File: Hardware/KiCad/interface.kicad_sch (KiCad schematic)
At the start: 34 parts, among them J1 USB_C, J2 STLink, J6 UART, J7 OLED, SW10 SW_Push_45deg, SW11 SW_Push_45deg, SW12 SW_Push_45deg, SW13 SW_Push_45deg, SW14 SW_Push_45deg, SW15 SW_Push_45deg, SW16 SW_Push_45deg, SW17 SW_Push_45deg, SW2 SW_Push_45deg, SW3 SW_Push_45deg, SW4 SW_Push_45deg, SW5 SW_Push_45deg, SW6 SW_Push_45deg, SW7 SW_Push_45deg, SW8 SW_Push_45deg, SW9 SW_Push_45deg, U1 USBLC6-2

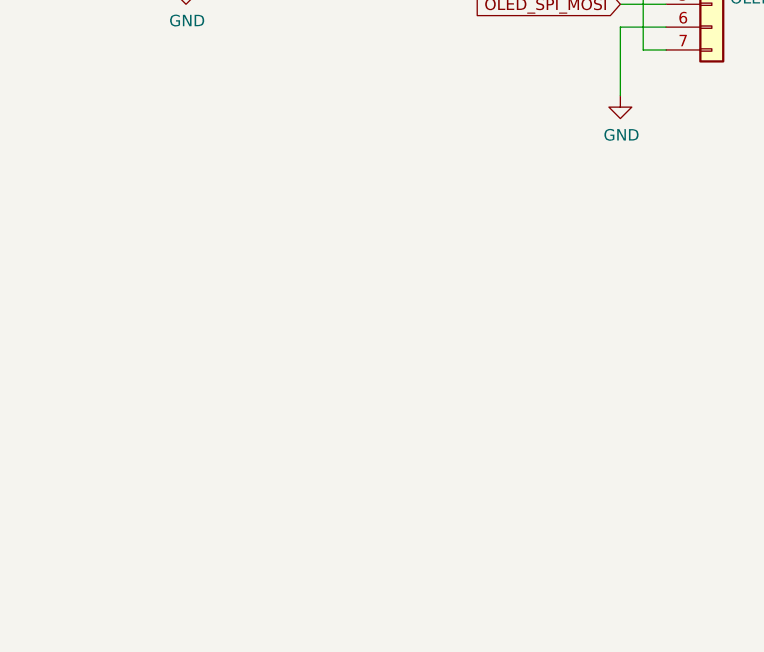
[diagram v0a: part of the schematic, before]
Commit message: add encoder & volume control, move SD_DET to accommodate encoder
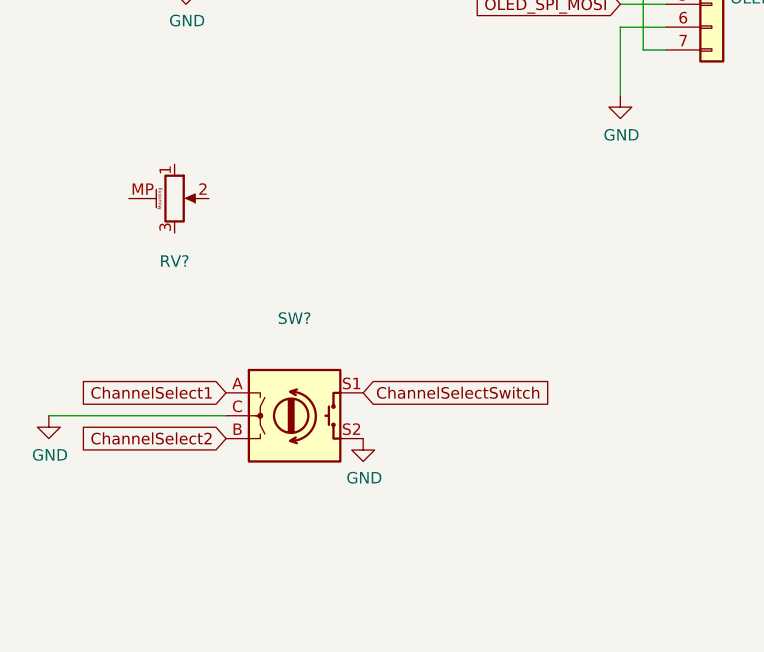
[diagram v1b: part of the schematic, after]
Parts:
- added RV?: (no value), symbol Device:R_Potentiometer_MountingPin
- added SW?: (no value), symbol Device:RotaryEncoder_Switch
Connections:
- net GND: now also SW?.C, SW?.S2
- new net ChannelSelect1: SW?.A
- new net ChannelSelect2: SW?.B
- new net ChannelSelectSwitch: SW?.S1
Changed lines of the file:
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@@
     (stroke (width 0) (type solid) (color 0 0 0 0))
+  )
+  (wire (pts (xy 25.4 91.44) (xy 45.085 91.44))
+    (stroke (width 0) (type default) (color 0 0 0 0))
   )
   (wire (pts (xy 58.42 143.51) (xy 58.42 156.21))
@@
     )
   )
+  (global_label "ChannelSelect2" (shape input) (at 45.085 93.98 180) (fields_autoplaced)
+    (effects (font (size 1.27 1.27)) (justify right))
+    (property "Intersheet References" "${INTERSHEET_REFS}" (id 0) (at 27.9762 93.9006 0)
+      (effects (font (size 1.27 1.27)) (justify right) hide)
+    )
+  )
   (global_label "C2" (shape output) (at 43.18 135.89 90) (fields_autoplaced)
     (effects (font (size 1.27 1.27)) (justify left))
@@
     )
   )
+  (global_label "ChannelSelectSwitch" (shape input) (at 60.325 88.9 0) (fields_autoplaced)
+    (effects (font (size 1.27 1.27)) (justify left))
+    (property "Intersheet References" "${INTERSHEET_REFS}" (id 0) (at 82.3324 88.8206 0)
+      (effects (font (size 1.27 1.27)) (justify left) hide)
+    )
+  )
   (global_label "OLED_SPI_MOSI" (shape input) (at 88.9 45.72 180) (fields_autoplaced)
     (effects (font (size 1.27 1.27)) (justify right))
@@
     )
   )
+  (global_label "ChannelSelect1" (shape input) (at 45.085 88.9 180) (fields_autoplaced)
+    (effects (font (size 1.27 1.27)) (justify right))
+    (property "Intersheet References" "${INTERSHEET_REFS}" (id 0) (at 27.9762 88.8206 0)
+      (effects (font (size 1.27 1.27)) (justify right) hide)
+    )
+  )
   (global_label "C1" (shape output) (at 27.94 135.89 90) (fields_autoplaced)
     (effects (font (size 1.27 1.27)) (justify left))
@@
     (pin "1")
     (pin "2")
+  )
+  (symbol (lib_id "Device:RotaryEncoder_Switch") (at 52.705 91.44 0) (unit 1)
+    (in_bom yes) (on_board yes) (fields_autoplaced)
+    (property "Reference" "SW?" (id 0) (at 52.705 80.645 0))
+    (property "Value" "" (id 1) (at 52.705 83.185 0))
+    (property "Footprint" "" (id 2) (at 48.895 87.376 0)
+      (effects (font (size 1.27 1.27)) hide)
+    )
+    (property "Datasheet" "https://www.cuidevices.com/product/resource/acz11.pdf" (id 3) (at 52.705 84.836 0)
+      (effects (font (size 1.27 1.27)) hide)
+    )
+    (pin "A")
+    (pin "B")
+    (pin "C")
+    (pin "S1")
+    (pin "S2")
   )
   (symbol (lib_id "power:VDD") (at 146.05 20.32 0) (unit 1)
@@
     (pin "2")
   )
+  (symbol (lib_id "Device:R_Potentiometer_MountingPin") (at 39.37 67.31 0) (unit 1)
+    (in_bom yes) (on_board yes)
+    (property "Reference" "RV?" (id 0) (at 39.37 74.295 0))
+    (property "Value" "" (id 1) (at 39.37 61.595 0))
+    (property "Footprint" "" (id 2) (at 39.37 67.31 0)
+      (effects (font (size 1.27 1.27)) hide)
+    )
+    (property "Datasheet" "https://datasheet.lcsc.com/lcsc/2005150044_ALPSALPINE-RK09L1140A2U_C470448.pdf" (id 3) (at 39.37 67.31 0)
+      (effects (font (size 1.27 1.27)) hide)
+    )
+    (pin "1")
+    (pin "2")
+    (pin "3")
+    (pin "MP")
+  )
   (symbol (lib_id "Switch:SW_Push_45deg") (at 60.96 171.45 0) (unit 1)
     (in_bom yes) (on_board yes) (fields_autoplaced)
@@
     (pin "2")
   )
+  (symbol (lib_id "power:GND") (at 60.325 93.98 0) (unit 1)
+    (in_bom yes) (on_board yes)
+    (property "Reference" "#PWR?" (id 0) (at 60.325 100.33 0)
+      (effects (font (size 1.27 1.27)) hide)
+    )
+    (property "Value" "GND" (id 1) (at 60.452 98.3742 0))
+    (property "Footprint" "" (id 2) (at 60.325 93.98 0)
+      (effects (font (size 1.27 1.27)) hide)
+    )
+    (property "Datasheet" "" (id 3) (at 60.325 93.98 0)
+      (effects (font (size 1.27 1.27)) hide)
+    )
+    (pin "1")
+  )
   (symbol (lib_id "power:GND") (at 166.37 40.64 0) (unit 1)
     (in_bom yes) (on_board yes)
@@
     (pin "2")
   )
+  (symbol (lib_id "power:GND") (at 25.4 91.44 0) (unit 1)
+    (in_bom yes) (on_board yes)
+    (property "Reference" "#PWR?" (id 0) (at 25.4 97.79 0)
+      (effects (font (size 1.27 1.27)) hide)
+    )
+    (property "Value" "GND" (id 1) (at 25.527 95.8342 0))
+    (property "Footprint" "" (id 2) (at 25.4 91.44 0)
+      (effects (font (size 1.27 1.27)) hide)
+    )
+    (property "Datasheet" "" (id 3) (at 25.4 91.44 0)
+      (effects (font (size 1.27 1.27)) hide)
+    )
+    (pin "1")
+  )
 )
